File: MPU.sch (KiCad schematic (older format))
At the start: 26 parts, among them P1 BL_PAD, P11 CONN_01X04, P2 SWD_DAT, P3 SWD_CLK, P4 SWD_3V3, P5 SWD_GND, P6 SWD_RST, SW1 SW_PUSH, SW2 SW_PUSH, U4 SAMD21E17A, Y1 32.768kHz

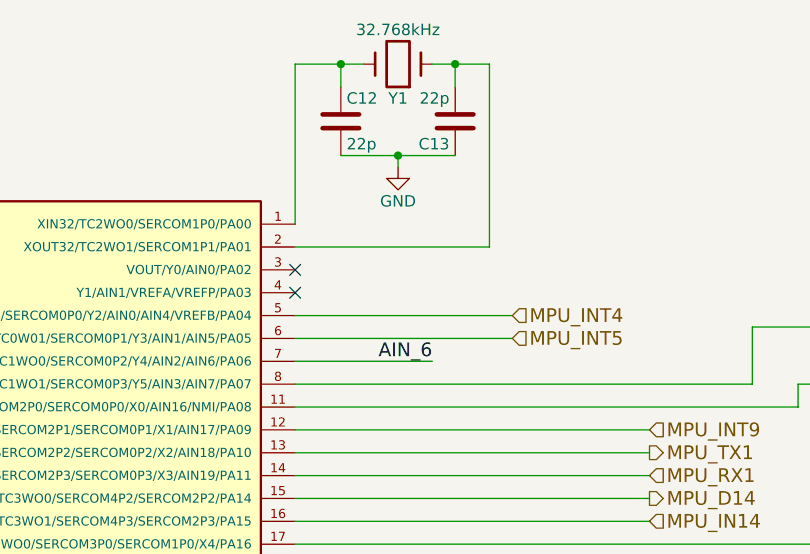
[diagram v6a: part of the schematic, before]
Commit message: Added USB monitoring resistors, still need to set values. Also added stitching vias and tried to clean up some layout
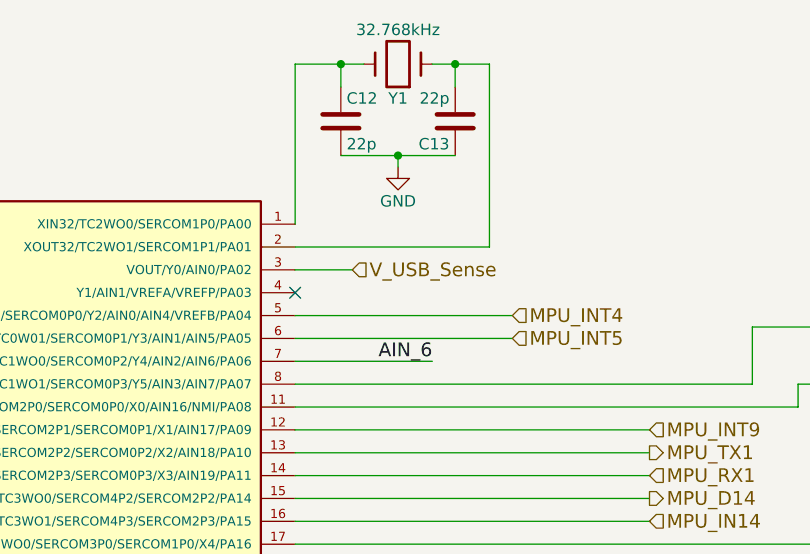
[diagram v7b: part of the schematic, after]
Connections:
- net V_USB_Sense: now reaches U4.3 (VOUT/Y0/AIN0/PA02)
- no-connect marks 2 -> 1
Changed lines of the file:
@@
 Connection ~ 2200 2050
 $Comp
-L GND #PWR013
+L GND #PWR15
 U 1 1 56C1336E
 P 1900 2650
-F 0 "#PWR013" H 1900 2400 50  0001 C CNN
+F 0 "#PWR15" H 1900 2400 50  0001 C CNN
 F 1 "GND" H 1900 2500 50  0000 C CNN
 F 2 "" H 1900 2650 50  0000 C CNN
@@
 $EndComp
 $Comp
-L GND #PWR014
+L GND #PWR16
 U 1 1 56C133A0
 P 2200 2650
-F 0 "#PWR014" H 2200 2400 50  0001 C CNN
+F 0 "#PWR16" H 2200 2400 50  0001 C CNN
 F 1 "GND" H 2200 2500 50  0000 C CNN
 F 2 "" H 2200 2650 50  0000 C CNN
@@
 $EndComp
 $Comp
-L GND #PWR015
+L GND #PWR18
 U 1 1 56C133D2
 P 2500 2650
-F 0 "#PWR015" H 2500 2400 50  0001 C CNN
+F 0 "#PWR18" H 2500 2400 50  0001 C CNN
 F 1 "GND" H 2500 2500 50  0000 C CNN
 F 2 "" H 2500 2650 50  0000 C CNN
@@
 $EndComp
 $Comp
-L +3V3 #PWR016
+L +3V3 #PWR30
 U 1 1 56C24D00
 P 9150 2500
-F 0 "#PWR016" H 9150 2350 50  0001 C CNN
+F 0 "#PWR30" H 9150 2350 50  0001 C CNN
 F 1 "+3V3" H 9150 2640 50  0000 C CNN
 F 2 "" H 9150 2500 50  0000 C CNN
@@
 $EndComp
 $Comp
-L GND #PWR017
+L GND #PWR25
 U 1 1 56C269FF
 P 6100 1400
-F 0 "#PWR017" H 6100 1150 50  0001 C CNN
+F 0 "#PWR25" H 6100 1150 50  0001 C CNN
 F 1 "GND" H 6100 1250 50  0000 C CNN
 F 2 "" H 6100 1400 50  0000 C CNN
@@
 AIN_6
 $Comp
-L GND #PWR018
+L GND #PWR21
 U 1 1 56C278AB
 P 4000 6000
-F 0 "#PWR018" H 4000 5750 50  0001 C CNN
+F 0 "#PWR21" H 4000 5750 50  0001 C CNN
 F 1 "GND" H 4000 5850 50  0000 C CNN
 F 2 "" H 4000 6000 50  0000 C CNN
@@
 	1550 3000 1550 3200
 $Comp
-L GND #PWR019
+L GND #PWR14
 U 1 1 56C282F2
 P 1550 3600
-F 0 "#PWR019" H 1550 3350 50  0001 C CNN
+F 0 "#PWR14" H 1550 3350 50  0001 C CNN
 F 1 "GND" H 1550 3450 50  0000 C CNN
 F 2 "" H 1550 3600 50  0000 C CNN
@@
 	1550 3500 1550 3600
 $Comp
-L +3V3 #PWR020
+L +3V3 #PWR13
 U 1 1 56C28419
 P 1550 3000
-F 0 "#PWR020" H 1550 2850 50  0001 C CNN
+F 0 "#PWR13" H 1550 2850 50  0001 C CNN
 F 1 "+3V3" H 1550 3140 50  0000 C CNN
 F 2 "" H 1550 3000 50  0000 C CNN
@@
 	2600 1650 2600 1550
 $Comp
-L +3V3 #PWR021
+L +3V3 #PWR19
 U 1 1 56C28F33
 P 2600 1150
-F 0 "#PWR021" H 2600 1000 50  0001 C CNN
+F 0 "#PWR19" H 2600 1000 50  0001 C CNN
 F 1 "+3V3" H 2600 1290 50  0000 C CNN
 F 2 "" H 2600 1150 50  0000 C CNN
@@
 	2600 1150 2600 1250
 $Comp
-L +3V3 #PWR022
+L +3V3 #PWR23
 U 1 1 56C2B080
 P 5350 5800
-F 0 "#PWR022" H 5350 5650 50  0001 C CNN
+F 0 "#PWR23" H 5350 5650 50  0001 C CNN
 F 1 "+3V3" H 5350 5940 50  0000 C CNN
 F 2 "" H 5350 5800 50  0000 C CNN
@@
 $EndComp
 $Comp
-L GND #PWR023
+L GND #PWR24
 U 1 1 56C2B0D0
 P 5350 6000
-F 0 "#PWR023" H 5350 5750 50  0001 C CNN
+F 0 "#PWR24" H 5350 5750 50  0001 C CNN
 F 1 "GND" H 5350 5850 50  0000 C CNN
 F 2 "" H 5350 6000 50  0000 C CNN
@@
 	5350 5950 6150 5950
 $Comp
-L +3V3 #PWR024
+L +3V3 #PWR17
 U 1 1 56C2B3B6
 P 2350 1900
-F 0 "#PWR024" H 2350 1750 50  0001 C CNN
+F 0 "#PWR17" H 2350 1750 50  0001 C CNN
 F 1 "+3V3" H 2350 2040 50  0000 C CNN
 F 2 "" H 2350 1900 50  0000 C CNN
@@
 Connection ~ 2350 2050
 $Comp
-L GND #PWR025
+L GND #PWR20
 U 1 1 56C39EB2
 P 2900 4300
-F 0 "#PWR025" H 2900 4050 50  0001 C CNN
+F 0 "#PWR20" H 2900 4050 50  0001 C CNN
 F 1 "GND" H 2900 4150 50  0000 C CNN
 F 2 "" H 2900 4300 50  0000 C CNN
@@
 	4700 6200 4700 6050
 $Comp
-L +3V3 #PWR026
+L +3V3 #PWR22
 U 1 1 56C3A13C
 P 4700 5100
-F 0 "#PWR026" H 4700 4950 50  0001 C CNN
+F 0 "#PWR22" H 4700 4950 50  0001 C CNN
 F 1 "+3V3" H 4700 5240 50  0000 C CNN
 F 2 "" H 4700 5100 50  0000 C CNN
@@
 Wire Wire Line
 	5050 6200 4700 6200
-NoConn ~ 5650 1850
 NoConn ~ 5650 1950
 Text HLabel 7200 2650 2    60   Output ~ 0
@@
 $EndComp
 $Comp
-L GND #PWR027
+L GND #PWR28
 U 1 1 56EAE5DD
 P 8450 4000
-F 0 "#PWR027" H 8450 3750 50  0001 C CNN
+F 0 "#PWR28" H 8450 3750 50  0001 C CNN
 F 1 "GND" H 8450 3850 50  0000 C CNN
 F 2 "" H 8450 4000 50  0000 C CNN
@@
 $EndComp
 $Comp
-L +3.3V #PWR028
+L +3.3V #PWR27
 U 1 1 56EAE62B
 P 8300 3350
-F 0 "#PWR028" H 8300 3200 50  0001 C CNN
+F 0 "#PWR27" H 8300 3200 50  0001 C CNN
 F 1 "+3.3V" H 8300 3490 50  0000 C CNN
 F 2 "" H 8300 3350 50  0000 C CNN
@@
 $EndComp
 $Comp
-L GND #PWR029
+L GND #PWR29
 U 1 1 56EC2766
 P 8750 2600
-F 0 "#PWR029" H 8750 2350 50  0001 C CNN
+F 0 "#PWR29" H 8750 2350 50  0001 C CNN
 F 1 "GND" H 8750 2450 50  0000 C CNN
 F 2 "" H 8750 2600 50  0000 C CNN
@@
 $EndComp
 $Comp
-L +3V3 #PWR030
+L +3V3 #PWR26
 U 1 1 56F90C8F
 P 6100 5000
-F 0 "#PWR030" H 6100 4850 50  0001 C CNN
+F 0 "#PWR26" H 6100 4850 50  0001 C CNN
 F 1 "+3V3" H 6100 5140 50  0000 C CNN
 F 2 "" H 6100 5000 50  0000 C CNN
@@
 Text HLabel 7200 4200 2    60   Input ~ 0
 Data+
+Text HLabel 5900 1850 2    60   Input ~ 0
+V_USB_Sense
+Wire Wire Line
+	5650 1850 5900 1850
 $EndSCHEMATC
